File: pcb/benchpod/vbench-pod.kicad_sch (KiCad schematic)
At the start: 111 parts, among them J1 PZ254V-12-22P, SW1 TS-1088-AR02016, SW2 TS-1088-AR02016, U1 ICE40UP5K-SG48ITR, U10 TCAN1044VDRBRQ1, U2 W25Q64JVSSIQ, U24 SN74LVC2G66DCUR, U28 SRV05-4.TCT, U4 ESP32-C3-MINI-1-N4, U5 STM32H563ZGT6, U7 APS6404L-3SQR-ZR, U8 TPS2116DRLR, X1 SX3M48.000B10F20TNN, Y2 6pF ±10ppm SMD2016-4P Crystal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

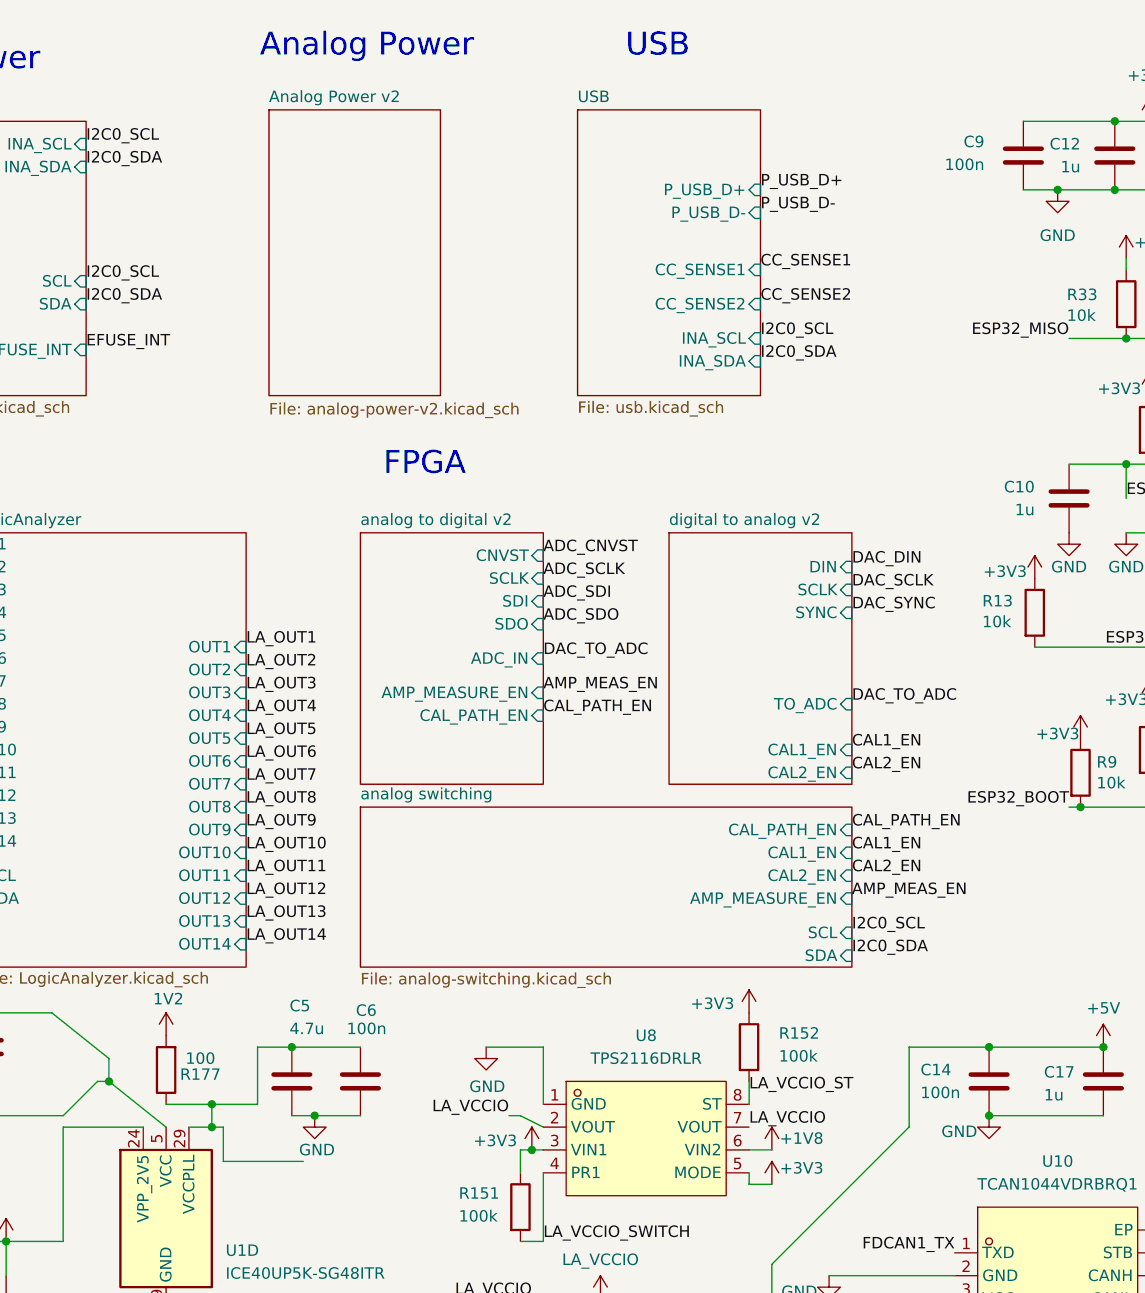
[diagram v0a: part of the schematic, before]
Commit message: analog v3r2: +-14 V (TPS65131) enabled from U58 P4, off by default
U49 ENP/ENN were pulled up to VIN, so +-14 V was always on. They now share
the new ANA14_EN net from the relay expander U58 P4 (TCA9554 0x23, spare
pin), with R114 (100k) as pull-down to GND; R117 removed. TPS65131 EN:
VIH 1.4 V, 0.1 uA, so the 3.3 V expander output and 100k pull-down work.

Why: the DAC8554 powers up at code 0, which put the +-12 V output (RF3) at
about -12 V until firmware parked channel C. With +-14 V off at power-up,
-14 V is 0 V and +14 V sits at ~VIN - Vf (no BSW load switch), so U51
cannot swing negative and RF3 stays near 0 V. Old firmware never enables
it, so on v3r2 the +-12 V output is simply off. It also stops the
TPS65131 switching noise whenever the +-12 V output is not in use.

Firmware: on v3r2, park DAC channel C at mid-scale, then set U58 P4 high.
Netlist diff = exactly the intended changes; ERC errors unchanged (25);
BOM 123 lines.

Co-Authored-By: Claude Opus 5.5 <noreply@anthropic.com>
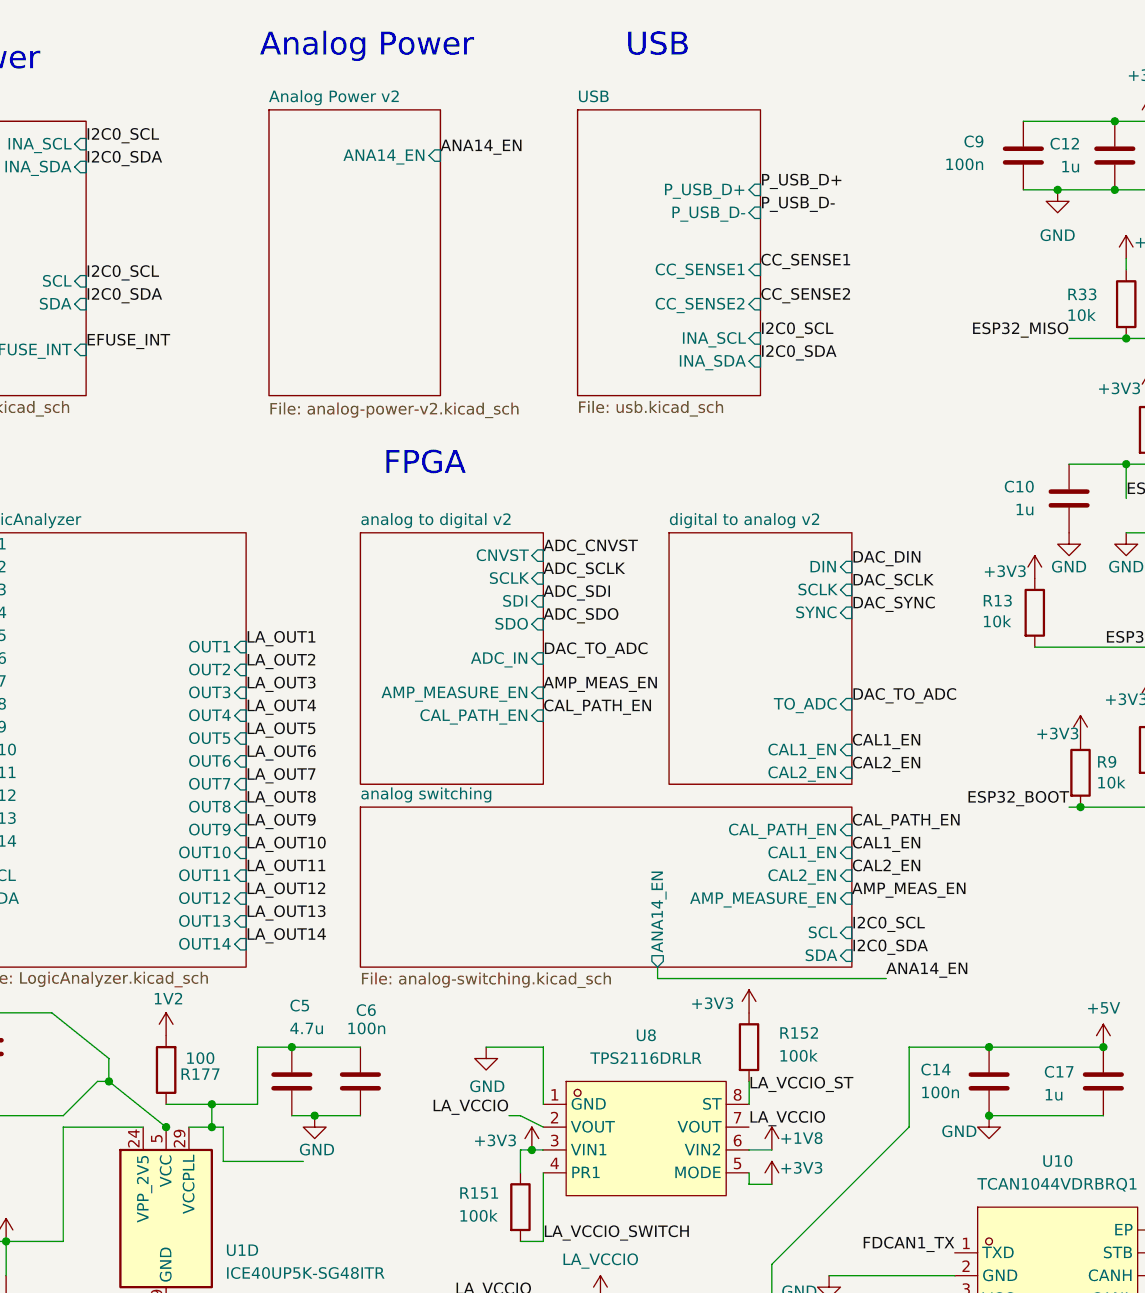
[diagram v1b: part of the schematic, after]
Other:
- sheet Analog Power v2 ports: added ANA14_EN; removed none
- sheet analog switching ports: added ANA14_EN; removed none
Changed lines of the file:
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@@
 	)
 	(junction
+		(at 46.99 138.43)
+		(diameter 0)
+		(color 0 0 0 0)
+	)
+	(junction
 		(at 96.52 172.72)
 		(diameter 0)
@@
 	(wire
 		(pts
+			(xy 101.6 120.65) (xy 101.6 121.92)
+		)
+		(stroke
+			(width 0)
+			(type default)
+		)
+	)
+	(wire
+		(pts
 			(xy 181.61 255.27) (xy 191.77 255.27)
 		)
@@
 	(wire
 		(pts
+			(xy 101.6 121.92) (xy 127 121.92)
+		)
+		(stroke
+			(width 0)
+			(type default)
+		)
+	)
+	(wire
+		(pts
 			(xy 288.29 137.16) (xy 303.53 137.16)
 		)
@@
 		)
 	)
+	(label "ANA14_EN"
+		(at 127 121.92 0)
+		(effects
+			(font
+				(size 1.27 1.27)
+			)
+			(justify left bottom)
+		)
+	)
 	(label "LA_INPUT1"
 		(at 193.04 176.53 180)
@@
 		)
 	)
+	(label "ANA14_EN"
+		(at 77.47 30.48 0)
+		(effects
+			(font
+				(size 1.27 1.27)
+			)
+			(justify left bottom)
+		)
+	)
 	(label "LA_OUT7"
 		(at 55.88 100.33 0)
@@
 			)
 		)
+		(pin "ANA14_EN" output
+			(at 101.6 120.65 270)
+			(effects
+				(font
+					(size 1.27 1.27)
+				)
+				(justify left)
+			)
+		)
 		(instances
 			(project "vbench-pod"
@@
 			)
 		)
+		(pin "ANA14_EN" input
+			(at 77.47 30.48 0)
+			(effects
+				(font
+					(size 1.27 1.27)
+				)
+				(justify right)
+			)
+		)
 		(instances
 			(project "vbench-pod"
@@
 		)
 	)
-	(embedded_fonts no)
 )

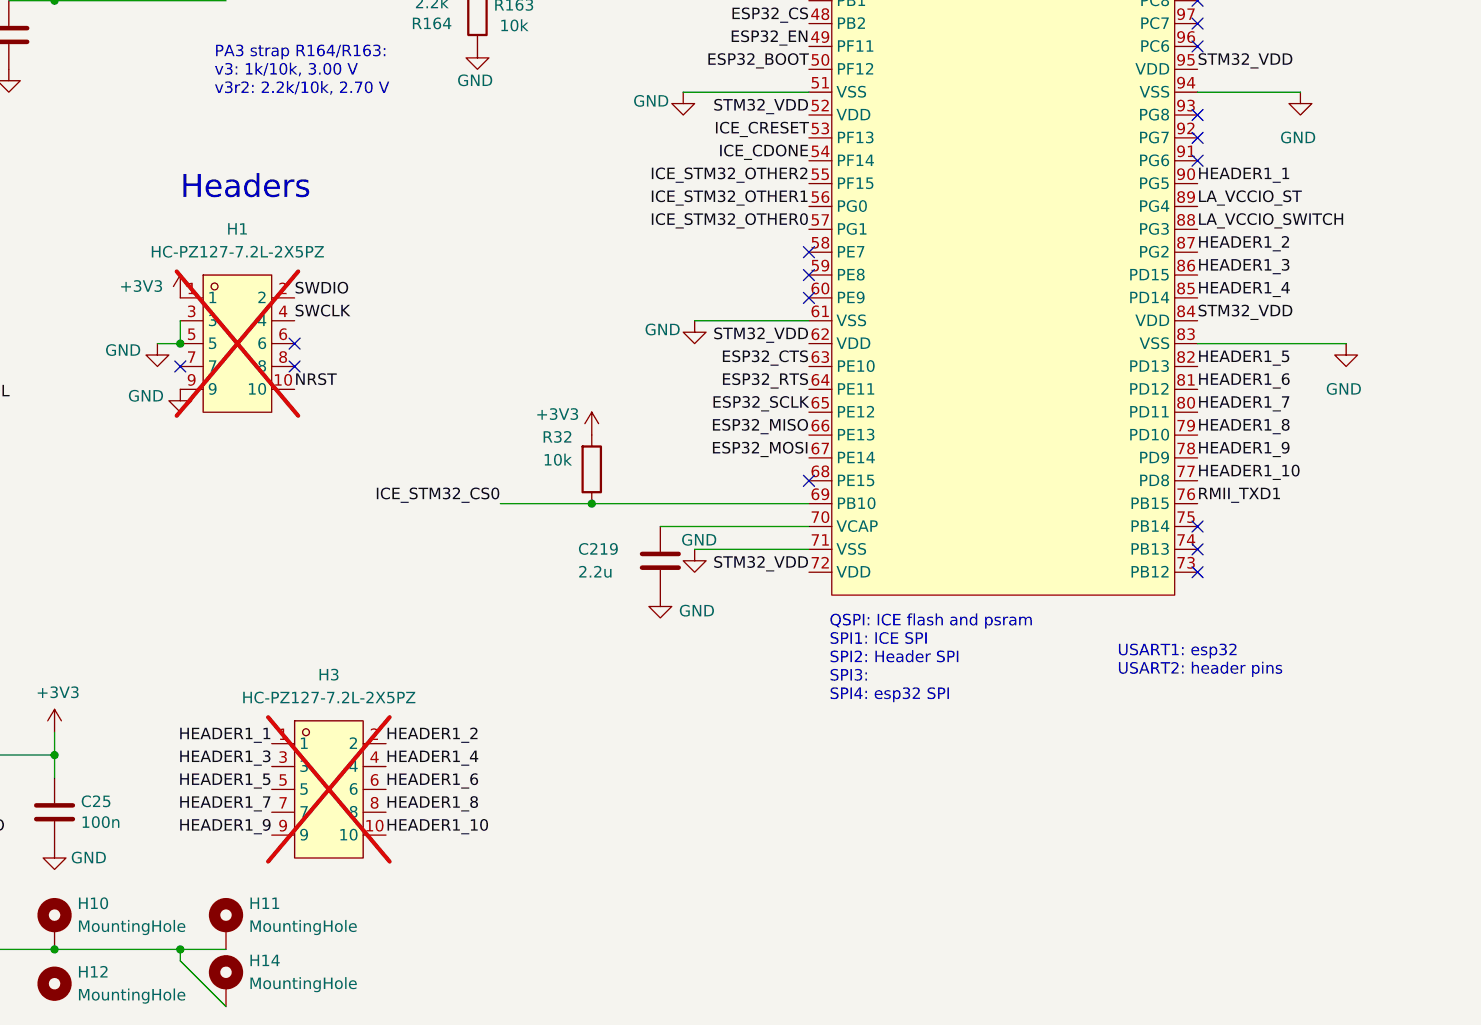
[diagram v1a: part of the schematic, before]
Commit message: analog v3r2: remove H3 (unused 2x5 GPIO header), freed STM32 pins no-connect
PD8-PD15, PG2, PG5 (HEADER1_1..10) get no-connect flags, like the pins
freed by the H2 removal. BOM lines unchanged (H1 still uses the same
header part until it becomes a TC2030 footprint).

Co-Authored-By: Claude Opus 5.5 <noreply@anthropic.com>
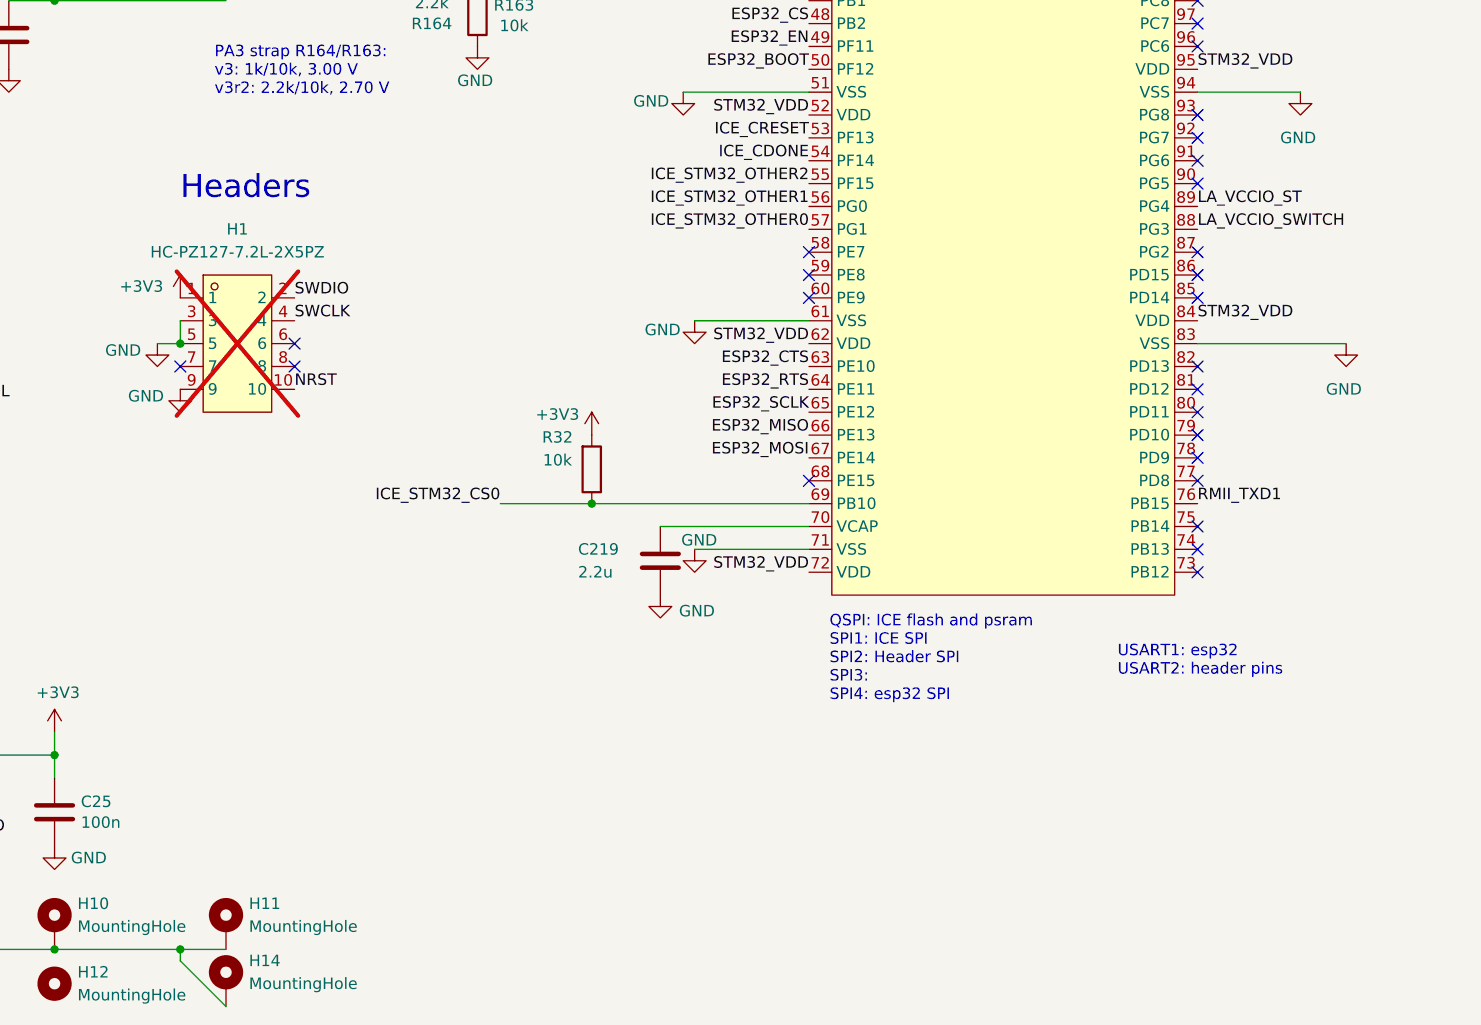
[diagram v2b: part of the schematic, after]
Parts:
- removed H3: HC-PZ127-7.2L-2X5PZ, lcsc:HDR-TH_HC-PZ127-7.2L-2X5PZ, symbol lcsc_lib:HC-PZ127-7.2L-2X5PZ
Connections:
- net HEADER1_1: no longer names the net of U5.90 (PG5)
- net HEADER1_10: no longer names the net of U5.77 (PD8)
- net HEADER1_2: no longer names the net of U5.87 (PG2)
- net HEADER1_3: no longer names the net of U5.86 (PD15)
- net HEADER1_4: no longer names the net of U5.85 (PD14)
- net HEADER1_5: no longer names the net of U5.82 (PD13)
- net HEADER1_6: no longer names the net of U5.81 (PD12)
- net HEADER1_7: no longer names the net of U5.80 (PD11)
- net HEADER1_8: no longer names the net of U5.79 (PD10)
- net HEADER1_9: no longer names the net of U5.78 (PD9)
- no-connect marks 67 -> 77
